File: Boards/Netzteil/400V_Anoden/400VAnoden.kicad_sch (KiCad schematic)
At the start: 50 parts, among them J1 Chassis_GND, P1 Drossel, P2 320V_AC, P3 Stabi, P4 133V_AC, P5 Stabi, P6 Trafo, P7 Trafo, P8 Relay, Q1 2SC2979

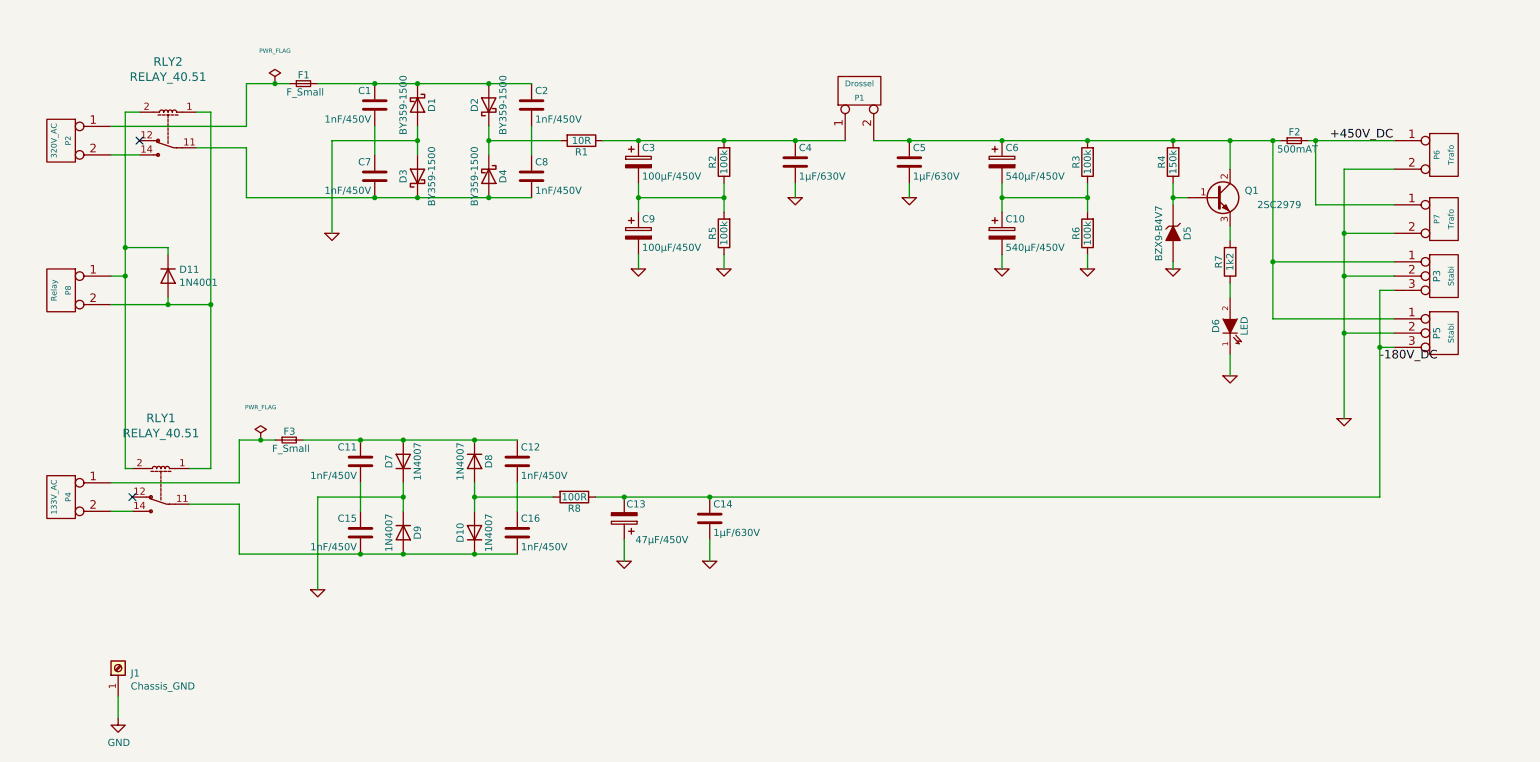
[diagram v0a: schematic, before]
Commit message: 6.3V, 400V und 400V Regler Boards bestellt
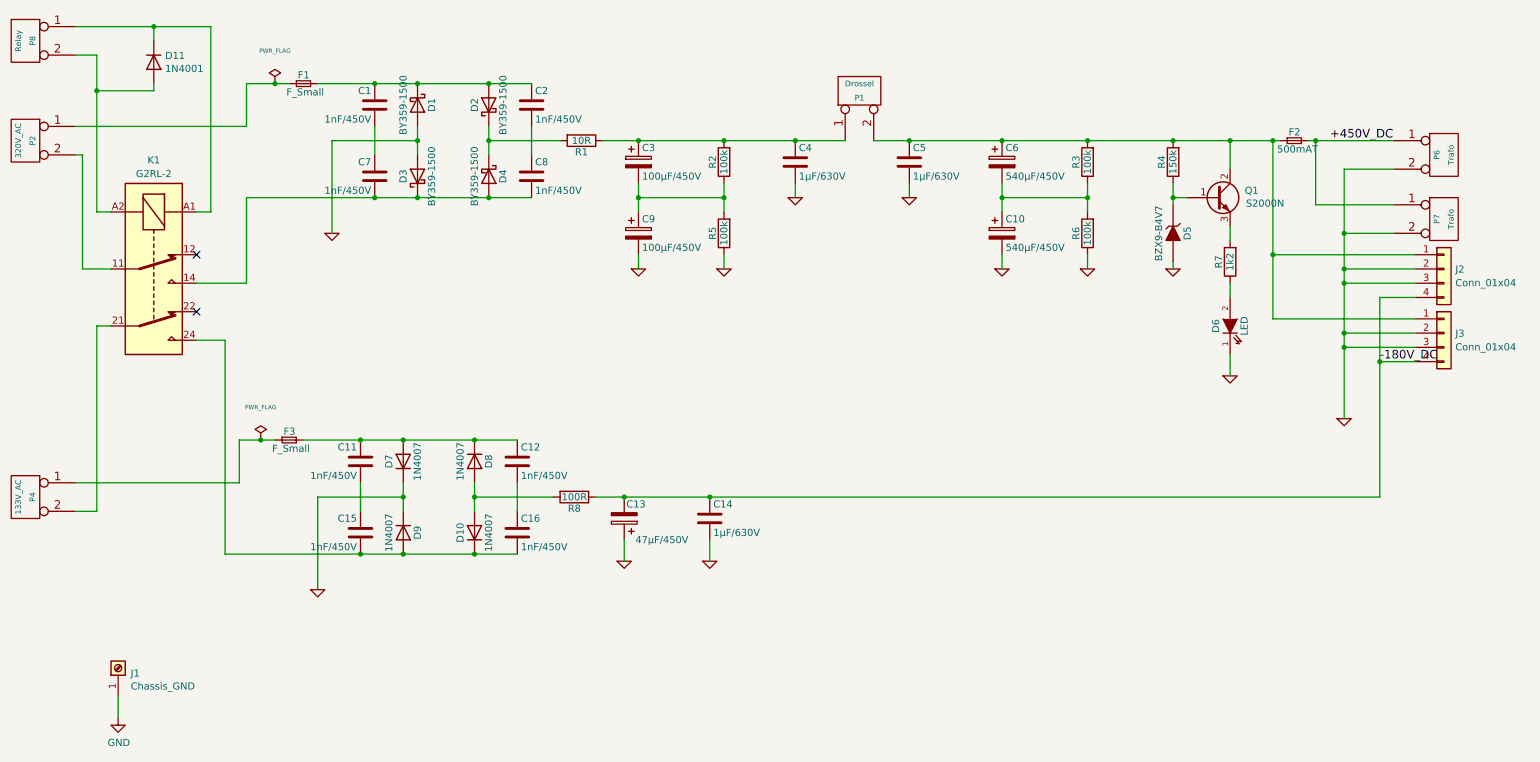
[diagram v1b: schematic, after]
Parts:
- removed P3: Stabi, Connector_TE-Connectivity:TE_MATE-N-LOK_1-770870-x_1x03_P4.14mm_Vertical, symbol 400VAnoden-rescue:CONN_3-borniers
- removed P5: Stabi, footprints:39302030, symbol 400VAnoden-rescue:CONN_3-borniers
- removed RLY1, RLY2: RELAY_40.51, w_relay:relay_40.51, symbol w_relay:RELAY_40.51
- added J2, J3: Conn_01x04, Connector_Molex:Molex_Mini-Fit_Jr_5566-04A_2x02_P4.20mm_Vertical, symbol Connector_Generic:Conn_01x04
- added K1: G2RL-2, Relay_THT:Relay_DPDT_Omron_G2RL-2, symbol Relay:G2RL-2
- F1, F2, F3: footprint w_misc_comp:fuse_holder_CQ-2 -> Fuse_Holder_Eska:Fuse__Holder_Eska_509100
- P1, P2, P4, P6, P7: footprint Connector_TE-Connectivity:TE_MATE-N-LOK_1-770866-x_1x02_P4.14mm_Vertical -> Connector_Molex:Molex_Mini-Fit_Jr_5566-02A_2x01_P4.20mm_Vertical
- Q1: value 2SC2979 -> S2000N; footprint Package_TO_SOT_THT:TO-220-3_Horizontal_TabDown -> Package_TO_SOT_THT:TO-3P-3_Horizontal_TabDown
- R7: footprint Resistor_THT:R_Axial_DIN0207_L6.3mm_D2.5mm_P10.16mm_Horizontal -> Resistor_THT:R_Axial_DIN0414_L11.9mm_D4.5mm_P15.24mm_Horizontal
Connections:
- net -180V_DC: now also J2.4 (Pin_4), J3.4 (Pin_4)
- net GND: now also J2.2 (Pin_2), J2.3 (Pin_3), J3.2 (Pin_2), J3.3 (Pin_3)
- net at P2.2 (P2): now also K1.11
- net at C5.1, C6.1, F2.1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: now also J2.1 (Pin_1), J3.1 (Pin_1)
- net at C7.2, C8.2, D3.1 (K)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: now also K1.14
- net at P4.2 (P2): now also K1.21
- net at C15.2, C16.2, D10.1 (K)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: now also K1.24
- net at D11.2 (A), P8.2 (P2): now also K1.A2
- net at D11.1 (K), P8.1 (P1): now also K1.A1
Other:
- moved on the sheet: D11, P2, P4, P8

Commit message: Leiterplatte erstellt
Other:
- note added: "10H / 400mA"
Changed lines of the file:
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@@
+		)
+	)
+	(text "10H / 400mA"
+		(exclude_from_sim no)
+		(at 169.164 49.784 0)
+		(effects
+			(font
+				(size 1.27 1.27)
+			)
 		)
 	)
